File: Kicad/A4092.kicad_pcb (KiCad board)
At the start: 4 copper layers, 175.6 x 122.1 mm, 107 parts, among them CN1 Zorro3, J1 Conn_02x25_Odd_Even, J2 Conn_01x06_Pin, J3 TO-LED, J4 TO-MB, J5 5787170-5, J7 22112042, J8 TO-A3000-LED, J9 TO-A3000-MB, SW1 219-8MST, U1 SN74ABT16543DGGR, U10 NCR53c710 SCSI Host Controller, U11 DS21S07A, U12 DS21S07A, U13 SST39SF010/020/040, U2 SN74ABT16543DGGR, U3 SN74ABT16543DGGR, U4 SN74ABT16543DGGR, U5 74LVC07APW_118, U6 SN74ABT16245ADGGR, U7 AMS1117-3.3, U8 SN74F244DB, U9 XC95144XL-TQ144, Y1 Abracon ACO-50MHz

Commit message: Routing
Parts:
- moved C36 8.51 mm to (123.5, 105.0)
- moved FB3 5.91 mm to (118.0, 98.0), turned to 180 degrees
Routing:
- net PLD_SID: track 121.3 -> 168.4 mm, vias 1 -> 2
- net D7: track 103.9 -> 145.6 mm, vias 1 -> 2
- net D6: track 103.0 -> 143.6 mm, vias 1 -> 2
- net PLD_MTCR: track 0.00 -> 38.3 mm
- net D25: track 61.5 -> 87.5 mm, vias 0 -> 1
- net D24: track 59.7 -> 83.8 mm, vias 0 -> 1
- net D27: track 70.2 -> 93.4 mm, vias 0 -> 1
- net D26: track 69.2 -> 88.9 mm, vias 0 -> 1
- net MASTER: track 59.2 -> 74.9 mm
- net A31: track 98.1 -> 90.7 mm
- net A28: track 102.7 -> 105.4 mm
- net IORST: track 135.9 -> 133.9 mm
- net A17: track 146.1 -> 144.2 mm
- net D1: track 117.0 -> 115.2 mm
- net D2: track 124.7 -> 123.2 mm
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
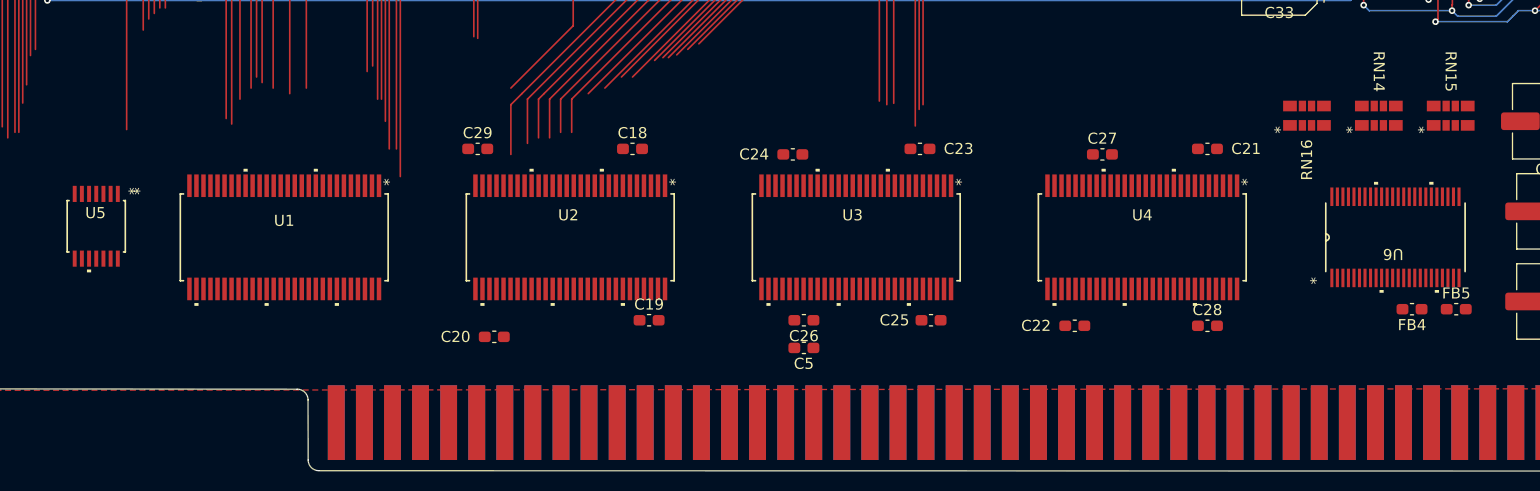
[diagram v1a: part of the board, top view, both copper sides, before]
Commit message: Move transceivers north
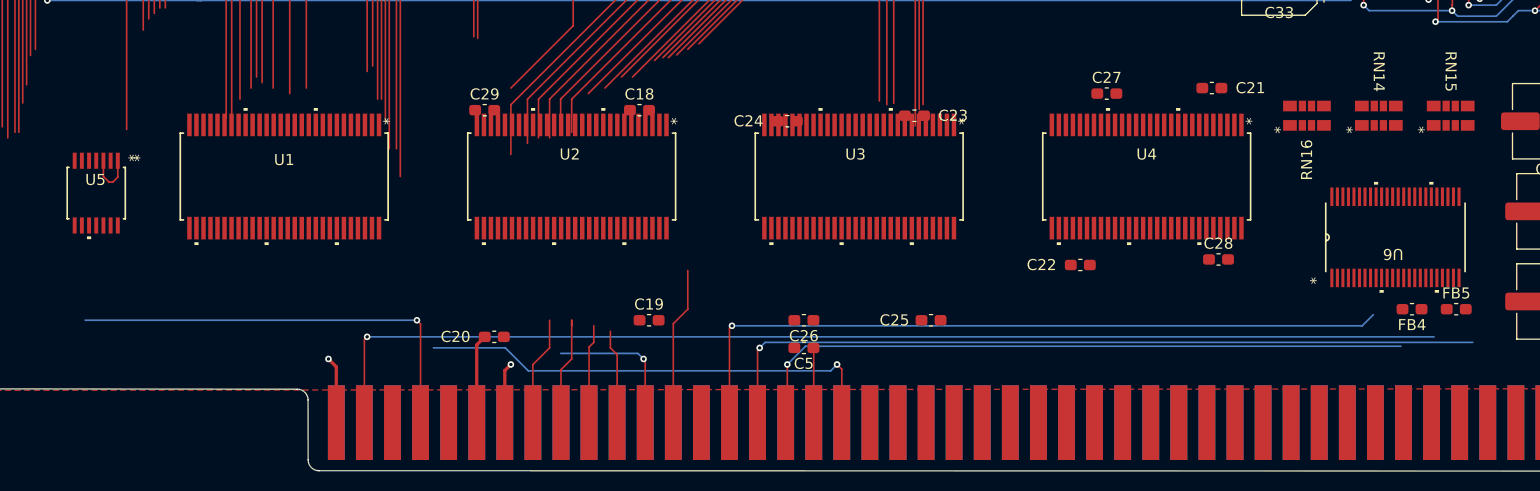
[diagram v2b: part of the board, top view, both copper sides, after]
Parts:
- moved C28 6.08 mm to (175.5, 135.5)
- moved C22 5.52 mm to (163.0, 136.0)
- moved C21 5.51 mm to (174.9, 120.0)
- moved C27 5.51 mm to (165.4, 120.5)
- moved U4 5.51 mm to (169.0, 128.0)
- moved U3 5.51 mm to (143.0, 128.0)
- moved U2 5.50 mm to (117.0, 128.0)
- moved U1 5.50 mm to (91.0, 128.0)
- moved C18 3.56 mm to (123.1, 122.0)
- moved C29 3.56 mm to (109.1, 122.0)
- moved C23 3.04 mm to (148.0, 122.5)
- moved C24 3.04 mm to (136.5, 123.0)
- moved U5 3.00 mm to (74.0, 129.5)
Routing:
- net Z_DS1: track 0.00 -> 104.4 mm, vias 0 -> 1
- net Z_DS2: track 0.00 -> 71.5 mm, vias 0 -> 1
- net Z_DS3: track 0.00 -> 67.3 mm, vias 0 -> 1
- net Z_READ: track 0.00 -> 61.5 mm, vias 0 -> 1
- net Z_BGn: track 9.64 -> 52.7 mm, vias 0 -> 1
- net Z_IORST: track 0.00 -> 39.4 mm, vias 0 -> 1
- net GND: track 136.6 -> 156.2 mm, vias 43 -> 45
- net Z_A26D26: track 0.00 -> 14.3 mm
- net Z_A25D25: track 0.00 -> 13.5 mm, vias 0 -> 1
- net Z_D22: track 0.00 -> 10.2 mm
- net Z_D21: track 0.00 -> 9.89 mm
- net Z_D23: track 0.00 -> 8.94 mm
- net Z_A24D24: track 0.00 -> 8.51 mm
- net Z_DTACK: track 31.7 -> 38.5 mm
- net SCSI_BUSY: track 0.00 -> 4.60 mm

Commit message: more routing
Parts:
- moved C25 6.02 mm to (150.0, 135.0)
- moved C23 3.61 mm to (151.0, 120.5)
- moved C24 2.69 mm to (135.5, 120.5)
- moved C29 1.73 mm to (110.0, 120.5)
- moved C18 1.54 mm to (123.5, 120.5)
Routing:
- net Z_MTACK: track 32.7 -> 98.7 mm, vias 0 -> 1
- net Z_BRn: track 26.8 -> 82.1 mm, vias 0 -> 1
- net Z_FCS: track 0.00 -> 26.9 mm
- net PLD_FC0: track 10.6 -> 36.7 mm
- net D29: track 94.0 -> 70.4 mm
- net D28: track 95.6 -> 72.3 mm
- net D27: track 93.4 -> 72.8 mm
- net Z_A19D11: track 0.00 -> 20.3 mm
- net D26: track 88.9 -> 68.9 mm
- net Z_A18D10: track 0.00 -> 19.8 mm
- net Z_A9D1: track 0.00 -> 18.9 mm
- net PLD_READ: track 38.6 -> 57.5 mm
- net DP3_ABRT: track 12.9 -> 30.4 mm, vias 1 -> 2
- net V5: track 72.8 -> 90.1 mm, vias 14 -> 20
- net D22: track 27.5 -> 10.3 mm
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
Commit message: Fix issues #12 and #13
Z_BEER and SCSI_BUSY were not connected correctly (single net pins)
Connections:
- CN1 pad 46: Z_BEER -> Z_BERR
- FL2 pad 5: Net-(J1-Pin_36) -> SCSI_BUSY
- J1 pad 36: Net-(J1-Pin_36) -> SCSI_BUSY
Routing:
- net Net-(J1-Pin_36): track 6.78 -> 0.00 mm
- net SCSI_BUSY: track 4.60 -> 11.4 mm

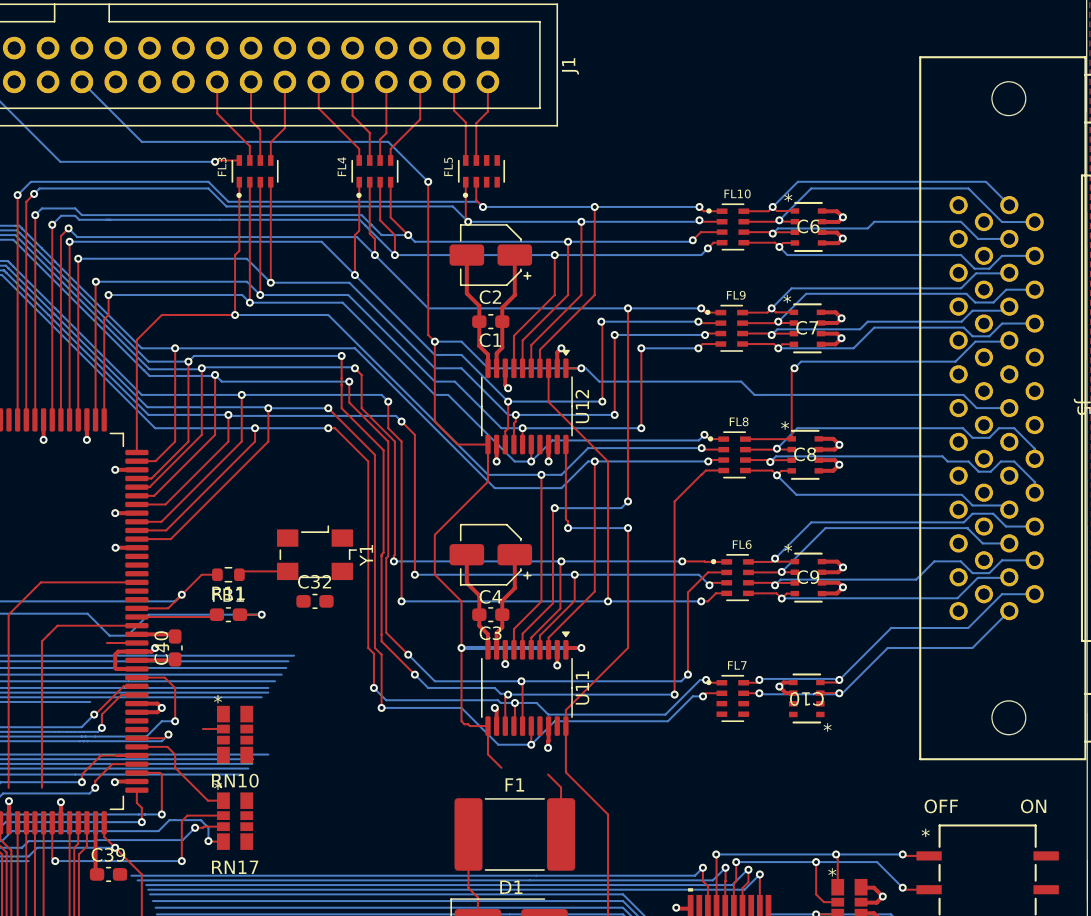
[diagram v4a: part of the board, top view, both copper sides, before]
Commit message: Feedback impleted for: [200~SCSI_TERMPWR traces should be 0.3mm min~
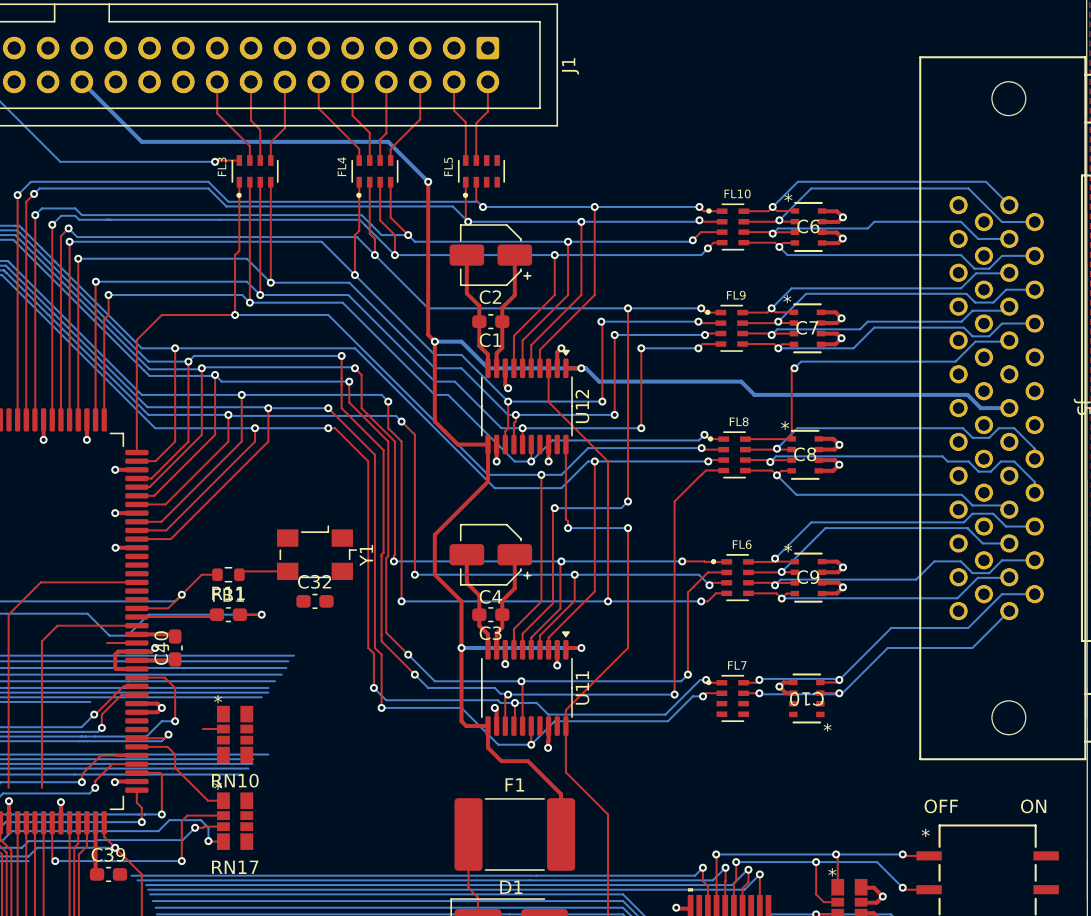
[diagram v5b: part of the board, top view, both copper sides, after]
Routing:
- net SCSI_TERMPWR: track 142.4 -> 145.6 mm
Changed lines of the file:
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@@
 		(start 175 60)
 		(end 175.5 60.5)
-		(width 0.15)
+		(width 0.3)
 		(layer "F.Cu")
 		(net 107)
@@
 	)
 	(segment
+		(start 177.8625 89.3625)
+		(end 177.5 89)
+		(width 0.3)
+		(layer "F.Cu")
+		(net 107)
+	)
+	(segment
 		(start 175.5 78)
 		(end 175.5 75)
-		(width 0.15)
+		(width 0.3)
+		(layer "F.Cu")
+		(net 107)
+	)
+	(segment
+		(start 177.5 89)
+		(end 177.5 83.5)
+		(width 0.3)
 		(layer "F.Cu")
 		(net 107)
@@
 		(start 185.3375 62.5)
 		(end 186.5 62.5)
-		(width 0.15)
+		(width 0.3)
 		(layer "F.Cu")
 		(net 107)
@@
 		(start 175 57)
 		(end 175 48.5)
-		(width 0.15)
-		(layer "F.Cu")
-		(net 107)
-	)
-	(segment
-		(start 180.5 92.5)
-		(end 179.4875 91.4875)
-		(width 0.15)
+		(width 0.3)
+		(layer "F.Cu")
+		(net 107)
+	)
+	(segment
+		(start 179.4875 90.9875)
+		(end 180.5 92)
+		(width 0.3)
 		(layer "F.Cu")
 		(net 107)
@@
 		(start 175.5 66.5)
 		(end 176.25 67.25)
-		(width 0.15)
-		(layer "F.Cu")
-		(net 107)
-	)
-	(segment
-		(start 177.725 89.225)
-		(end 177.5 89)
-		(width 0.15)
-		(layer "F.Cu")
-		(net 107)
-	)
-	(segment
-		(start 184.975 97.5)
-		(end 184.975 93.975)
-		(width 0.15)
+		(width 0.3)
 		(layer "F.Cu")
 		(net 107)
@@
 	)
 	(segment
+		(start 180.5 92)
+		(end 182.5 92)
+		(width 0.3)
+		(layer "F.Cu")
+		(net 107)
+	)
+	(segment
 		(start 179.4875 71.0125)
 		(end 179.4875 68.225)
-		(width 0.15)
-		(layer "F.Cu")
-		(net 107)
-	)
-	(segment
-		(start 179.4875 91.4875)
-		(end 179.4875 89.3625)
-		(width 0.15)
-		(layer "F.Cu")
-		(net 107)
-	)
-	(segment
-		(start 178 89.225)
-		(end 177.725 89.225)
-		(width 0.15)
+		(width 0.3)
 		(layer "F.Cu")
 		(net 107)
@@
 		(start 175 57)
 		(end 175 60)
-		(width 0.15)
+		(width 0.3)
 		(layer "F.Cu")
 		(net 107)
@@
 		(start 175.5 60.5)
 		(end 175.5 66.5)
-		(width 0.15)
+		(width 0.3)
+		(layer "F.Cu")
+		(net 107)
+	)
+	(segment
+		(start 179.4875 89.3625)
+		(end 179.4875 90.9875)
+		(width 0.3)
 		(layer "F.Cu")
 		(net 107)
@@
 		(start 177.5 83.5)
 		(end 177.5 80)
-		(width 0.15)
-		(layer "F.Cu")
-		(net 107)
-	)
-	(segment
-		(start 184.975 93.975)
-		(end 184 93)
-		(width 0.15)
-		(layer "F.Cu")
-		(net 107)
-	)
-	(segment
-		(start 177.5 89)
-		(end 177.5 83.5)
-		(width 0.15)
+		(width 0.3)
 		(layer "F.Cu")
 		(net 107)
@@
 	(segment
 		(start 179.4875 89.3625)
-		(end 178.1375 89.3625)
-		(width 0.15)
+		(end 177.8625 89.3625)
+		(width 0.3)
+		(layer "F.Cu")
+		(net 107)
+	)
+	(segment
+		(start 182.5 92)
+		(end 184.975 94.475)
+		(width 0.3)
+		(layer "F.Cu")
+		(net 107)
+	)
+	(segment
+		(start 184.975 94.475)
+		(end 184.975 97.5)
+		(width 0.3)
 		(layer "F.Cu")
 		(net 107)
@@
 		(start 177.5 80)
 		(end 175.5 78)
-		(width 0.15)
-		(layer "F.Cu")
-		(net 107)
-	)
-	(segment
-		(start 178.1375 89.3625)
-		(end 178 89.225)
-		(width 0.15)
+		(width 0.3)
 		(layer "F.Cu")
 		(net 107)
@@
 		(start 179.4875 68.225)
 		(end 177.225 68.225)
-		(width 0.15)
+		(width 0.3)
 		(layer "F.Cu")
 		(net 107)
@@
 		(start 175.5 75)
 		(end 179.4875 71.0125)
-		(width 0.15)
+		(width 0.3)
 		(layer "F.Cu")
 		(net 107)
@@
 		(start 177.225 68.225)
 		(end 176.25 67.25)
-		(width 0.15)
+		(width 0.3)
 		(layer "F.Cu")
 		(net 107)
@@
 		(drill 0.3)
 		(layers "F.Cu" "B.Cu")
+		(net 107)
+	)
+	(segment
+		(start 175 48.5)
+		(end 172 45.5)
+		(width 0.3)
+		(layer "B.Cu")
+		(net 107)
+	)
+	(segment
+		(start 179.5 62.5)
+		(end 177.5 60.5)
+		(width 0.3)
+		(layer "B.Cu")
+		(net 107)
+	)
+	(segment
+		(start 198.5 63.5)
+		(end 199.5 64.5)
+		(width 0.3)
+		(layer "B.Cu")
+		(net 107)
+	)
+	(segment
+		(start 172 45.5)
+		(end 153.5 45.5)
+		(width 0.3)
+		(layer "B.Cu")
 		(net 107)
 	)
@@
 		(start 187.8375 63.5)
 		(end 198.5 63.5)
-		(width 0.15)
-		(layer "B.Cu")
-		(net 107)
-	)
-	(segment
-		(start 175 48.5)
-		(end 172 45.5)
-		(width 0.15)
-		(layer "B.Cu")
-		(net 107)
-	)
-	(segment
-		(start 179.5 62.5)
-		(end 177.5 60.5)
-		(width 0.15)
-		(layer "B.Cu")
-		(net 107)
-	)
-	(segment
-		(start 216.180191 65.49)
+		(width 0.3)
+		(layer "B.Cu")
+		(net 107)
+	)
+	(segment
+		(start 186.5 62.5)
+		(end 179.5 62.5)
+		(width 0.3)
+		(layer "B.Cu")
+		(net 107)
+	)
+	(segment
+		(start 153.5 45.5)
+		(end 149 41)
+		(width 0.3)
+		(layer "B.Cu")
+		(net 107)
+	)
+	(segment
+		(start 177.5 60.5)
+		(end 175.5 60.5)
+		(width 0.3)
+		(layer "B.Cu")
+		(net 107)
+	)
+	(segment
+		(start 216.5 65.5)
+		(end 216.51 65.49)
+		(width 0.3)
+		(layer "B.Cu")
+		(net 107)
+	)
+	(segment
+		(start 186.5 62.5)
+		(end 186.8375 62.5)
+		(width 0.3)
+		(layer "B.Cu")
+		(net 107)
+	)
+	(segment
+		(start 216.51 65.49)
 		(end 218.63 65.49)
-		(width 0.15)
-		(layer "B.Cu")
-		(net 107)
-	)
-	(segment
-		(start 172 45.5)
-		(end 153.5 45.5)
-		(width 0.15)
+		(width 0.3)
+		(layer "B.Cu")
+		(net 107)
+	)
+	(segment
+		(start 215.5 64.5)
+		(end 216.5 65.5)
+		(width 0.3)
+		(layer "B.Cu")
+		(net 107)
+	)
+	(segment
+		(start 199.5 64.5)
+		(end 215.5 64.5)
+		(width 0.3)
 		(layer "B.Cu")
 		(net 107)
@@
 		(start 186.8375 62.5)
 		(end 187.8375 63.5)
-		(width 0.15)
-		(layer "B.Cu")
-		(net 107)
-	)
-	(segment
-		(start 186.5 62.5)
-		(end 179.5 62.5)
-		(width 0.15)
-		(layer "B.Cu")
-		(net 107)
-	)
-	(segment
-		(start 153.5 45.5)
-		(end 149 41)
-		(width 0.15)
-		(layer "B.Cu")
-		(net 107)
-	)
-	(segment
-		(start 198.5 63.5)
-		(end 199.5 64.5)
-		(width 0.15)
-		(layer "B.Cu")
-		(net 107)
-	)
-	(segment
-		(start 177.5 60.5)
-		(end 175.5 60.5)
-		(width 0.15)
-		(layer "B.Cu")
-		(net 107)
-	)
-	(segment
-		(start 186.5 62.5)
-		(end 186.8375 62.5)
-		(width 0.15)
-		(layer "B.Cu")
-		(net 107)
-	)
-	(segment
-		(start 199.5 64.5)
-		(end 215.190191 64.5)
-		(width 0.15)
+		(width 0.3)
 		(layer "B.Cu")
 		(net 107)
@@
 		(layer "B.Cu")
 		(net 107)
-	)
-	(segment
-		(start 215.190191 64.5)
-		(end 216.180191 65.49)
-		(width 0.15)
-		(layer "B.Cu")
-		(net 107)

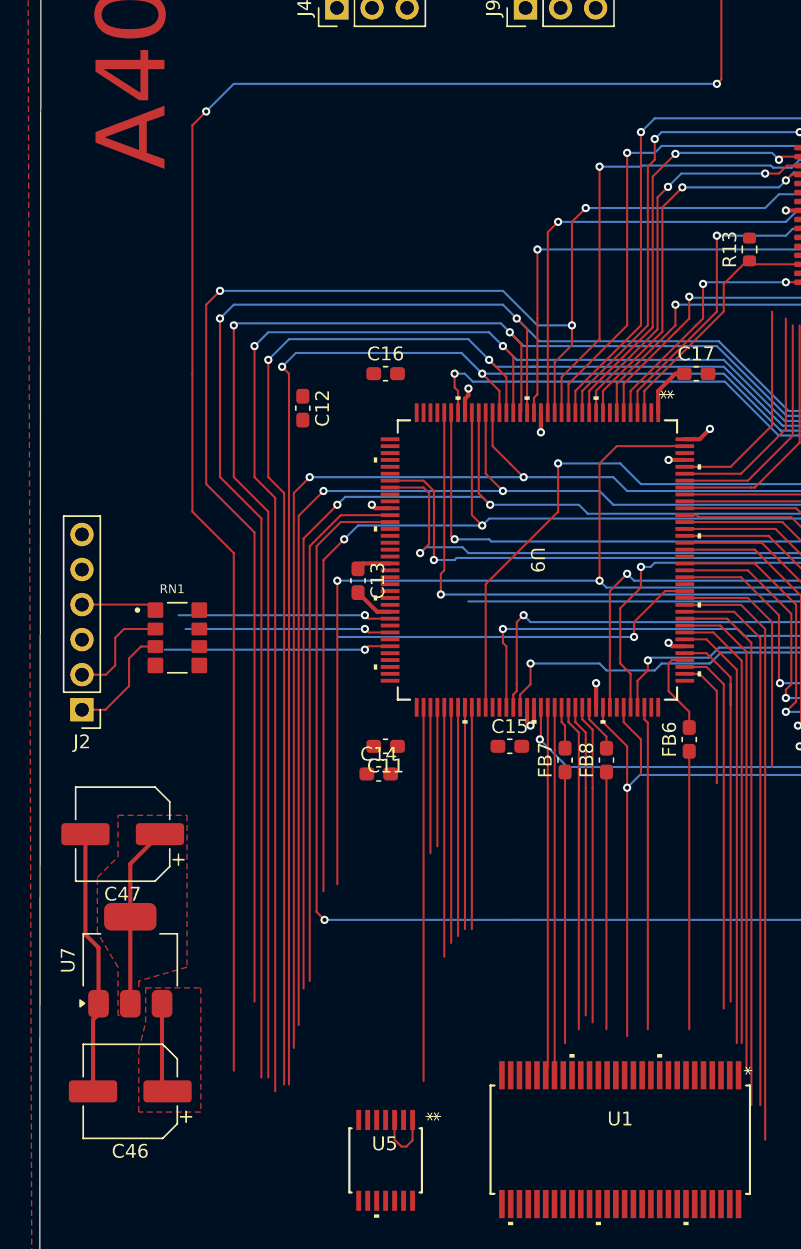
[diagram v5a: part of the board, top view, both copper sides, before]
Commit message: Feedback implemented:Make sure card guides don't hit components on the left side
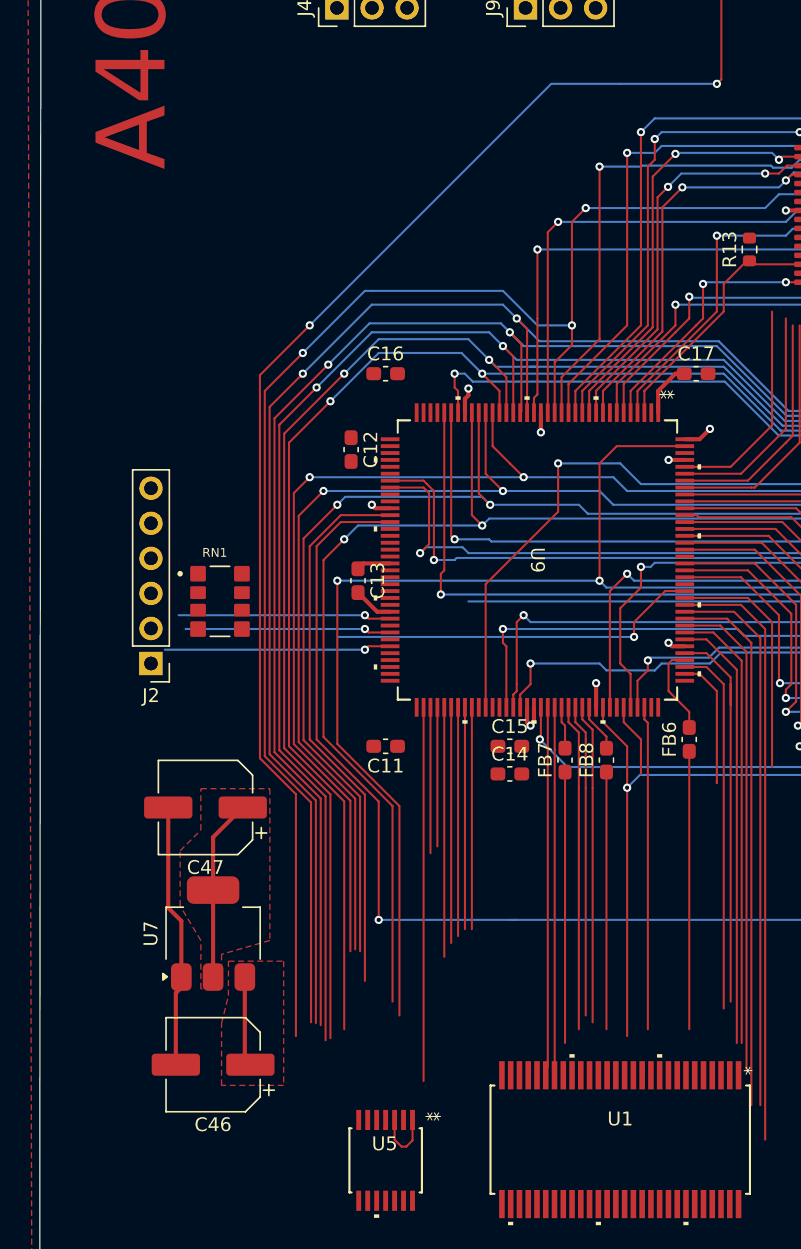
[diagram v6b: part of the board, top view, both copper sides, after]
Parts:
- moved C14 9.50 mm to (83.0, 101.5)
- moved C46 6.30 mm to (61.5, 122.6)
- moved U7 6.30 mm to (61.5, 113.1)
- moved C47 6.30 mm to (61.0, 103.9)
- moved J2 6.02 mm to (57.0, 93.5)
- moved C12 4.61 mm to (71.5, 78.0)
- moved RN1 4.06 mm to (62.0, 89.0)
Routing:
- net LED: track 120.0 -> 101.9 mm
- net IORST: track 133.9 -> 145.2 mm
- net A23: track 128.4 -> 117.3 mm
- net A24: track 128.4 -> 118.1 mm
- net A31: track 90.7 -> 100.8 mm
- net TMS: track 23.3 -> 14.9 mm
- net A25: track 125.6 -> 117.5 mm
- net TDI: track 23.3 -> 15.4 mm
- net A26: track 124.5 -> 117.8 mm
- net A17: track 144.2 -> 137.7 mm
- net A27: track 119.4 -> 113.1 mm
- net TCK: track 21.9 -> 16.4 mm
- net A28: track 105.4 -> 100.1 mm
- net A29: track 99.5 -> 95.7 mm
- net PLD_SID: track 168.4 -> 166.1 mm
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
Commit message: Routing in progress
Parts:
- moved RN16 11.7 mm to (193.5, 116.5)
- moved C12 1.50 mm to (71.5, 76.5)
- moved C21 1.10 mm to (176.0, 120.0)
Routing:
- net MASTER: track 66.9 -> 129.4 mm, vias 2 -> 3
- net Z_7M: track 0.00 -> 48.8 mm
- net PLD_DOE: track 0.00 -> 43.2 mm
- net A2: track 113.2 -> 156.0 mm
- net A3: track 112.9 -> 155.6 mm
- net A5: track 120.5 -> 163.0 mm
- net A4: track 112.0 -> 154.5 mm
- net A6: track 122.8 -> 165.1 mm
- net A7: track 121.0 -> 163.2 mm
- net DBOE: track 19.6 -> 57.0 mm
- net DBLT: track 26.6 -> 63.9 mm
- net GND: track 169.9 -> 201.2 mm, vias 48 -> 61
- net A10: track 55.7 -> 86.5 mm
- net A9: track 73.0 -> 103.3 mm
- net A8: track 116.5 -> 145.5 mm
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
